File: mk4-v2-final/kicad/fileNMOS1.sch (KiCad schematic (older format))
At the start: 4 parts, among them Q1 Q_NMOS_GDS

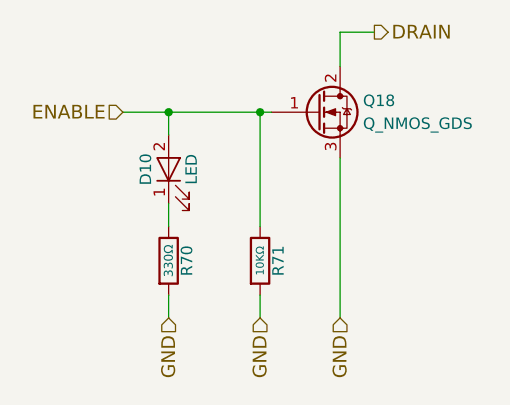
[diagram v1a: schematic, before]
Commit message: added headnight diodes, I don't think software control of them is going to be possible
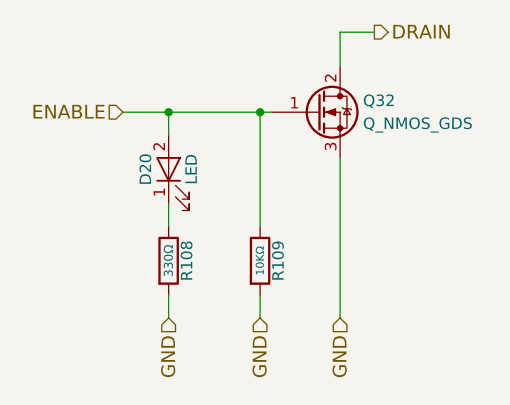
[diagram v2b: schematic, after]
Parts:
- renumbered D1 to D6, Q1 to Q7, R25 to R36, R26 to R37
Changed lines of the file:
@@
 ENABLE
 $Comp
-L R R26
+L R R37
 U 1 1 59DF0BE3
 P 5150 4900
-AR Path="/59DEA30F/5A0A2090/59DF0BE3" Ref="R26"  Part="1"
-AR Path="/59DEA30F/5A0A20A2/59DF0BE3" Ref="R28"  Part="1"
-AR Path="/59DEA30F/5A0A207D/59DF0BE3" Ref="R39"  Part="1"
-AR Path="/59DEA30F/5A282667/59DF0BE3" Ref="R69"  Part="1"
-AR Path="/59DEA30F/5A286B4A/59DF0BE3" Ref="R71"  Part="1"
-AR Path="/59DEA30F/5A1AB869/59DF0BE3" Ref="R73"  Part="1"
-AR Path="/59DEA30F/5A1AE2F5/59DF0BE3" Ref="R75"  Part="1"
-AR Path="/59DEA30F/5B17D435/59DF0BE3" Ref="R71"  Part="1"
-AR Path="/59DEA30F/5B17FE95/59DF0BE3" Ref="R71"  Part="1"
-F 0 "R71" V 5230 4900 50  0000 C CNN
+AR Path="/59DEA30F/5A0A207D/59DF0BE3" Ref="R37"  Part="1"
+AR Path="/59DEA30F/5A1AB869/59DF0BE3" Ref="R62"  Part="1"
+AR Path="/59DEA30F/5A1AE2F5/59DF0BE3" Ref="R64"  Part="1"
+AR Path="/59DEA30F/5B17D435/59DF0BE3" Ref="R107"  Part="1"
+AR Path="/59DEA30F/5B17FE95/59DF0BE3" Ref="R109"  Part="1"
+F 0 "R109" V 5230 4900 50  0000 C CNN
 F 1 "10KΩ" V 5150 4900 35  0000 C CNN
 F 2 "Resistors_THT:R_Axial_DIN0207_L6.3mm_D2.5mm_P10.16mm_Horizontal" V 5080 4900 50  0001 C CNN
@@
 GND
 $Comp
-L LED D1
+L LED D6
 U 1 1 5A613552
 P 4750 4500
-AR Path="/59DEA30F/5A0A2090/5A613552" Ref="D1"  Part="1"
-AR Path="/59DEA30F/5A0A20A2/5A613552" Ref="D2"  Part="1"
-AR Path="/59DEA30F/5A0A207D/5A613552" Ref="D5"  Part="1"
-AR Path="/59DEA30F/5A282667/5A613552" Ref="D9"  Part="1"
-AR Path="/59DEA30F/5A286B4A/5A613552" Ref="D10"  Part="1"
-AR Path="/59DEA30F/5A1AB869/5A613552" Ref="D11"  Part="1"
-AR Path="/59DEA30F/5A1AE2F5/5A613552" Ref="D12"  Part="1"
-AR Path="/59DEA30F/5B17D435/5A613552" Ref="D10"  Part="1"
-AR Path="/59DEA30F/5B17FE95/5A613552" Ref="D10"  Part="1"
-F 0 "D10" H 4750 4600 50  0000 C CNN
+AR Path="/59DEA30F/5A0A207D/5A613552" Ref="D6"  Part="1"
+AR Path="/59DEA30F/5A1AB869/5A613552" Ref="D9"  Part="1"
+AR Path="/59DEA30F/5A1AE2F5/5A613552" Ref="D10"  Part="1"
+AR Path="/59DEA30F/5B17D435/5A613552" Ref="D19"  Part="1"
+AR Path="/59DEA30F/5B17FE95/5A613552" Ref="D20"  Part="1"
+F 0 "D20" H 4750 4600 50  0000 C CNN
 F 1 "LED" H 4750 4400 50  0000 C CNN
 F 2 "LEDs:LED_D5.0mm" H 4750 4500 50  0001 C CNN
@@
 Connection ~ 4750 4250
 $Comp
-L R R25
+L R R36
 U 1 1 5A61355D
 P 4750 4900
-AR Path="/59DEA30F/5A0A2090/5A61355D" Ref="R25"  Part="1"
-AR Path="/59DEA30F/5A0A20A2/5A61355D" Ref="R27"  Part="1"
-AR Path="/59DEA30F/5A0A207D/5A61355D" Ref="R38"  Part="1"
-AR Path="/59DEA30F/5A282667/5A61355D" Ref="R68"  Part="1"
-AR Path="/59DEA30F/5A286B4A/5A61355D" Ref="R70"  Part="1"
-AR Path="/59DEA30F/5A1AB869/5A61355D" Ref="R72"  Part="1"
-AR Path="/59DEA30F/5A1AE2F5/5A61355D" Ref="R74"  Part="1"
-AR Path="/59DEA30F/5B17D435/5A61355D" Ref="R70"  Part="1"
-AR Path="/59DEA30F/5B17FE95/5A61355D" Ref="R70"  Part="1"
-F 0 "R70" V 4830 4900 50  0000 C CNN
+AR Path="/59DEA30F/5A0A207D/5A61355D" Ref="R36"  Part="1"
+AR Path="/59DEA30F/5A1AB869/5A61355D" Ref="R61"  Part="1"
+AR Path="/59DEA30F/5A1AE2F5/5A61355D" Ref="R63"  Part="1"
+AR Path="/59DEA30F/5B17D435/5A61355D" Ref="R106"  Part="1"
+AR Path="/59DEA30F/5B17FE95/5A61355D" Ref="R108"  Part="1"
+F 0 "R108" V 4830 4900 50  0000 C CNN
 F 1 "330Ω" V 4750 4900 39  0000 C CNN
 F 2 "Resistors_THT:R_Axial_DIN0207_L6.3mm_D2.5mm_P10.16mm_Horizontal" V 4680 4900 50  0001 C CNN
@@
 	5500 4450 5500 5150
 $Comp
-L Q_NMOS_GDS Q1
+L Q_NMOS_GDS Q7
 U 1 1 5A2ED2FC
 P 5400 4250
-AR Path="/59DEA30F/5A0A2090/5A2ED2FC" Ref="Q1"  Part="1"
-AR Path="/59DEA30F/5A0A20A2/5A2ED2FC" Ref="Q5"  Part="1"
-AR Path="/59DEA30F/5A0A207D/5A2ED2FC" Ref="Q9"  Part="1"
-AR Path="/59DEA30F/5A282667/5A2ED2FC" Ref="Q16"  Part="1"
-AR Path="/59DEA30F/5A286B4A/5A2ED2FC" Ref="Q18"  Part="1"
-AR Path="/59DEA30F/5A1AB869/5A2ED2FC" Ref="Q19"  Part="1"
-AR Path="/59DEA30F/5A1AE2F5/5A2ED2FC" Ref="Q20"  Part="1"
-AR Path="/59DEA30F/5B17D435/5A2ED2FC" Ref="Q18"  Part="1"
-AR Path="/59DEA30F/5B17FE95/5A2ED2FC" Ref="Q18"  Part="1"
-F 0 "Q18" H 5600 4300 50  0000 L CNN
+AR Path="/59DEA30F/5A0A207D/5A2ED2FC" Ref="Q7"  Part="1"
+AR Path="/59DEA30F/5A1AB869/5A2ED2FC" Ref="Q12"  Part="1"
+AR Path="/59DEA30F/5A1AE2F5/5A2ED2FC" Ref="Q13"  Part="1"
+AR Path="/59DEA30F/5B17D435/5A2ED2FC" Ref="Q31"  Part="1"
+AR Path="/59DEA30F/5B17FE95/5A2ED2FC" Ref="Q32"  Part="1"
+F 0 "Q32" H 5600 4300 50  0000 L CNN
 F 1 "Q_NMOS_GDS" H 5600 4200 50  0000 L CNN
 F 2 "TO_SOT_Packages_THT:TO-220-3_Vertical" H 5600 4350 50  0001 C CNN

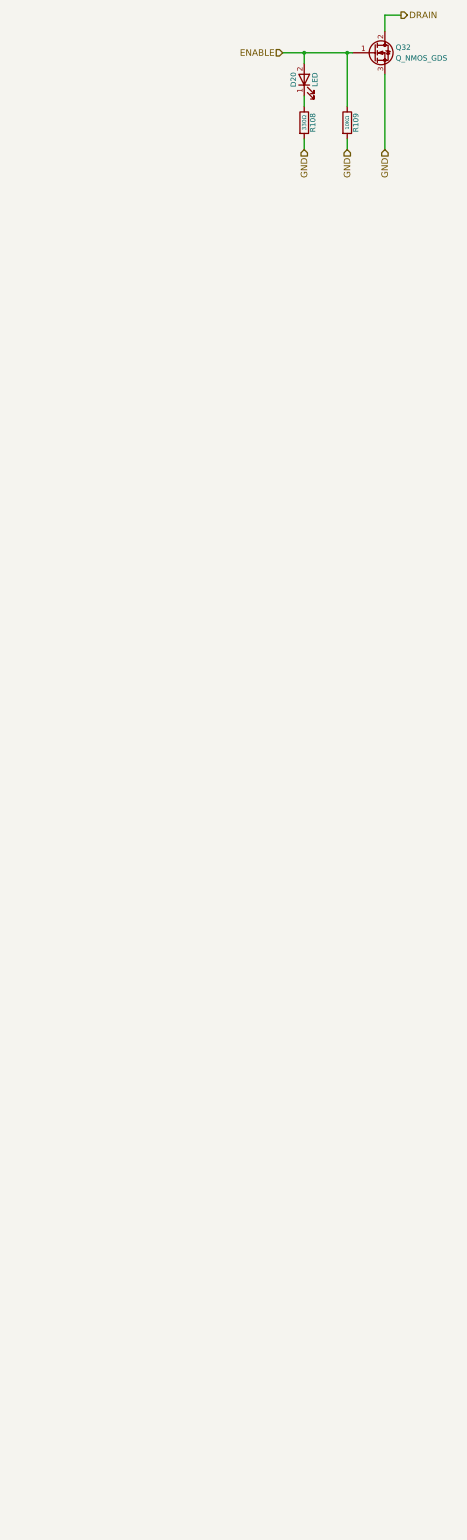
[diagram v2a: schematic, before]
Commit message: schematic is done, footprint association and netlist are also done
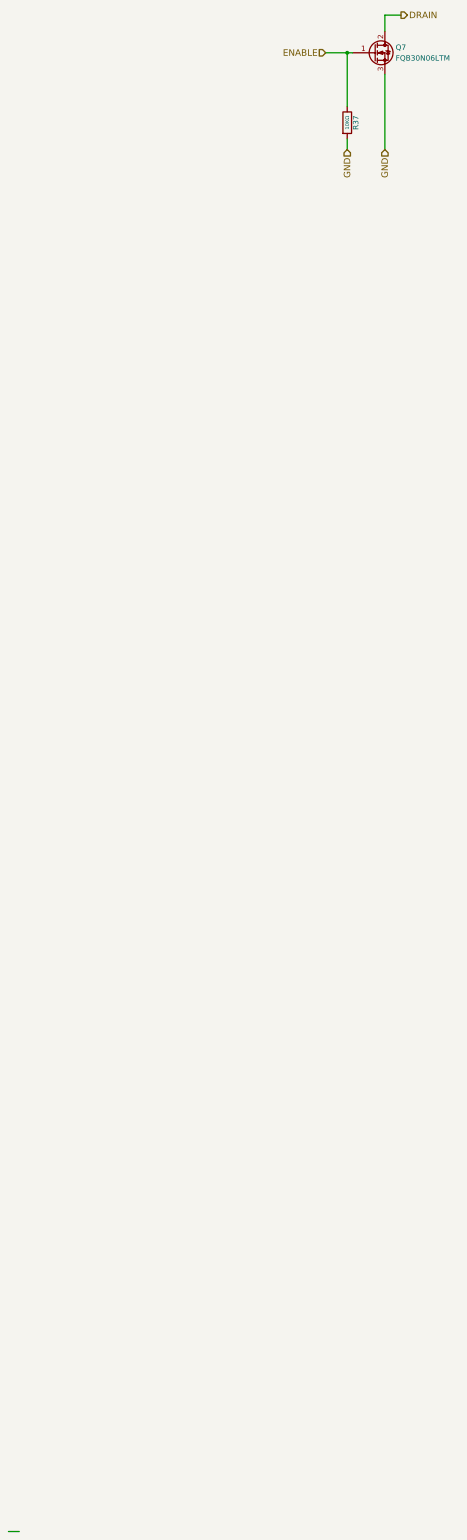
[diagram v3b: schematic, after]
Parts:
- removed D6: LED, LEDs:LED_D5.0mm, symbol LED
- removed R36: 330Ω, Resistors_THT:R_Axial_DIN0207_L6.3mm_D2.5mm_P10.16mm_Horizontal, symbol R
- Q7: value Q_NMOS_GDS -> FQB30N06LTM; footprint TO_SOT_Packages_THT:TO-220-3_Vertical -> TO_SOT_Packages_SMD:TO-263-3_TabPin2; digikey-pn (none) -> FQB30N06LTMCT-ND; mfg-pn (none) -> FQB30N06LTM
- R37: footprint Resistors_THT:R_Axial_DIN0207_L6.3mm_D2.5mm_P10.16mm_Horizontal -> Resistors_THT:R_Axial_DIN0204_L3.6mm_D1.6mm_P5.08mm_Horizontal; digikey-pn (none) -> BC10.0KXCT-ND; mfg-pn (none) -> MBA02040C1002FRP00
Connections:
- wire segments 9 -> 7
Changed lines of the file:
@@
 EESchema Schematic File Version 2
-LIBS:hitchco-mk4-rescue
 LIBS:power
 LIBS:device
@@
 LIBS:cd4013b
 LIBS:ncs3s1205sc
+LIBS:lca715
+LIBS:SN74HC595N
+LIBS:CD74HC4067
 LIBS:hitchco-mk4-cache
 EELAYER 25 0
@@
 $Descr USLetter 11000 8500
 encoding utf-8
-Sheet 12 54
+Sheet 15 54
 Title "sensor-mcu"
 Date "2017-10-11"
@@
 Comment4 ""
 $EndDescr
-Text HLabel 4550 4250 0    60   Input ~ 0
-ENABLE
 $Comp
 L R R37
@@
 AR Path="/59DEA30F/5B17D435/59DF0BE3" Ref="R107"  Part="1"
 AR Path="/59DEA30F/5B17FE95/59DF0BE3" Ref="R109"  Part="1"
-F 0 "R109" V 5230 4900 50  0000 C CNN
+F 0 "R37" V 5230 4900 50  0000 C CNN
 F 1 "10KΩ" V 5150 4900 35  0000 C CNN
-F 2 "Resistors_THT:R_Axial_DIN0207_L6.3mm_D2.5mm_P10.16mm_Horizontal" V 5080 4900 50  0001 C CNN
+F 2 "Resistors_THT:R_Axial_DIN0204_L3.6mm_D1.6mm_P5.08mm_Horizontal" V 5080 4900 50  0001 C CNN
 F 3 "" H 5150 4900 50  0001 C CNN
+F 4 "BC10.0KXCT-ND" H 5230 5000 50  0001 C CNN "digikey-pn"
+F 5 "MBA02040C1002FRP00" H 5230 5000 50  0001 C CNN "mfg-pn"
 	1    5150 4900
 	1    0    0    -1
 $EndComp
-Text HLabel 5650 3900 2    60   Output ~ 0
-DRAIN
-Wire Wire Line
-	4550 4250 5200 4250
-Wire Wire Line
-	5150 4250 5150 4750
-Connection ~ 5150 4250
-Wire Wire Line
-	5650 3900 5500 3900
-Wire Wire Line
-	5500 3900 5500 4050
-Text HLabel 5500 5150 3    60   Input ~ 0
-GND
-Text HLabel 5150 5150 3    60   Input ~ 0
-GND
-$Comp
-L LED D6
-U 1 1 5A613552
-P 4750 4500
-AR Path="/59DEA30F/5A0A207D/5A613552" Ref="D6"  Part="1"
-AR Path="/59DEA30F/5A1AB869/5A613552" Ref="D9"  Part="1"
-AR Path="/59DEA30F/5A1AE2F5/5A613552" Ref="D10"  Part="1"
-AR Path="/59DEA30F/5B17D435/5A613552" Ref="D19"  Part="1"
-AR Path="/59DEA30F/5B17FE95/5A613552" Ref="D20"  Part="1"
-F 0 "D20" H 4750 4600 50  0000 C CNN
-F 1 "LED" H 4750 4400 50  0000 C CNN
-F 2 "LEDs:LED_D5.0mm" H 4750 4500 50  0001 C CNN
-F 3 "http://www.kingbrightusa.com/images/catalog/SPEC/WP7113ID.pdf" H 4750 4500 50  0001 C CNN
-	1    4750 4500
-	0    -1   -1   0
-$EndComp
-Text HLabel 4750 5150 3    60   Input ~ 0
-GND
-Wire Wire Line
-	4750 4650 4750 4750
-Wire Wire Line
-	4750 4350 4750 4250
-Connection ~ 4750 4250
-$Comp
-L R R36
-U 1 1 5A61355D
-P 4750 4900
-AR Path="/59DEA30F/5A0A207D/5A61355D" Ref="R36"  Part="1"
-AR Path="/59DEA30F/5A1AB869/5A61355D" Ref="R61"  Part="1"
-AR Path="/59DEA30F/5A1AE2F5/5A61355D" Ref="R63"  Part="1"
-AR Path="/59DEA30F/5B17D435/5A61355D" Ref="R106"  Part="1"
-AR Path="/59DEA30F/5B17FE95/5A61355D" Ref="R108"  Part="1"
-F 0 "R108" V 4830 4900 50  0000 C CNN
-F 1 "330Ω" V 4750 4900 39  0000 C CNN
-F 2 "Resistors_THT:R_Axial_DIN0207_L6.3mm_D2.5mm_P10.16mm_Horizontal" V 4680 4900 50  0001 C CNN
-F 3 "" H 4750 4900 50  0001 C CNN
-	1    4750 4900
-	1    0    0    -1
-$EndComp
-Wire Wire Line
-	4750 5050 4750 5150
-Wire Wire Line
-	5150 5150 5150 5050
-Wire Wire Line
-	5500 4450 5500 5150
 $Comp
 L Q_NMOS_GDS Q7
@@
 AR Path="/59DEA30F/5B17D435/5A2ED2FC" Ref="Q31"  Part="1"
 AR Path="/59DEA30F/5B17FE95/5A2ED2FC" Ref="Q32"  Part="1"
-F 0 "Q32" H 5600 4300 50  0000 L CNN
-F 1 "Q_NMOS_GDS" H 5600 4200 50  0000 L CNN
-F 2 "TO_SOT_Packages_THT:TO-220-3_Vertical" H 5600 4350 50  0001 C CNN
-F 3 "" H 5400 4250 50  0001 C CNN
+F 0 "Q7" H 5600 4300 50  0000 L CNN
+F 1 "FQB30N06LTM" H 5600 4200 50  0000 L CNN
+F 2 "TO_SOT_Packages_SMD:TO-263-3_TabPin2" H 5600 4350 50  0001 C CNN
+F 3 "https://www.fairchildsemi.com/datasheets/FQ/FQB30N06L.pdf" H 5400 4250 50  0001 C CNN
+F 4 "FQB30N06LTMCT-ND" H 5600 4400 50  0001 C CNN "digikey-pn"
+F 5 "FQB30N06LTM" H 5600 4400 50  0001 C CNN "mfg-pn"
 	1    5400 4250
 	1    0    0    -1
 $EndComp
+Text HLabel 4950 4250 0    60   Input ~ 0
+ENABLE
+Text HLabel 5650 3900 2    60   Output ~ 0
+DRAIN
+Text HLabel 5500 5150 3    60   Input ~ 0
+GND
+Text HLabel 5150 5150 3    60   Input ~ 0
+GND
+Wire Wire Line
+	5150 4250 5150 4750
+Wire Wire Line
+	5650 3900 5500 3900
+Wire Wire Line
+	5500 3900 5500 4050
+Wire Wire Line
+	5150 5150 5150 5050
+Wire Wire Line
+	5500 4450 5500 5150
+Wire Wire Line
+	2000 18000 2100 18000
+Wire Wire Line
+	4950 4250 5200 4250
+Connection ~ 5150 4250
 $EndSCHEMATC

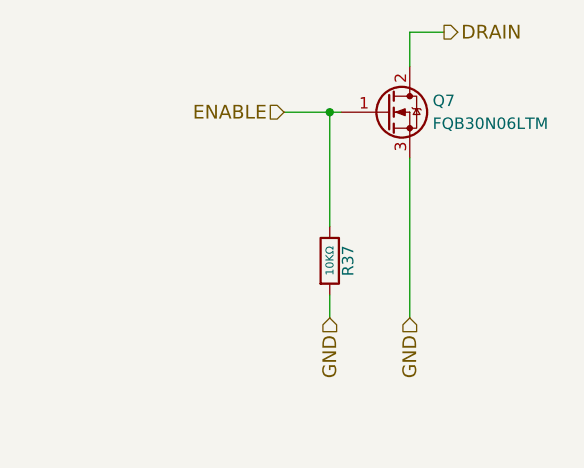
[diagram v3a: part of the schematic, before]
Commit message: all components on the board
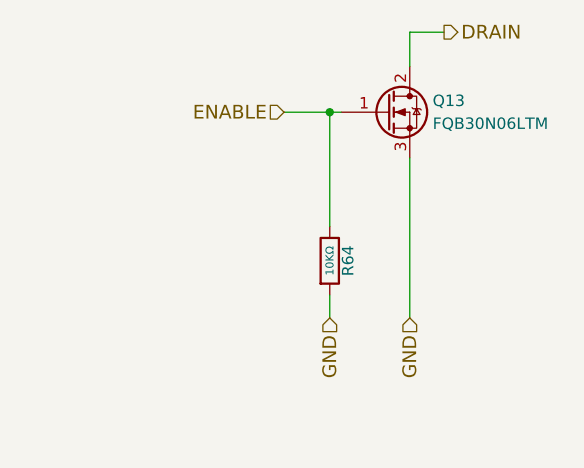
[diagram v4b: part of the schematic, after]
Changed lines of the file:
@@
 AR Path="/59DEA30F/5B17D435/59DF0BE3" Ref="R107"  Part="1"
 AR Path="/59DEA30F/5B17FE95/59DF0BE3" Ref="R109"  Part="1"
-F 0 "R37" V 5230 4900 50  0000 C CNN
+F 0 "R64" V 5230 4900 50  0000 C CNN
 F 1 "10KΩ" V 5150 4900 35  0000 C CNN
 F 2 "Resistors_THT:R_Axial_DIN0204_L3.6mm_D1.6mm_P5.08mm_Horizontal" V 5080 4900 50  0001 C CNN
@@
 AR Path="/59DEA30F/5B17D435/5A2ED2FC" Ref="Q31"  Part="1"
 AR Path="/59DEA30F/5B17FE95/5A2ED2FC" Ref="Q32"  Part="1"
-F 0 "Q7" H 5600 4300 50  0000 L CNN
+F 0 "Q13" H 5600 4300 50  0000 L CNN
 F 1 "FQB30N06LTM" H 5600 4200 50  0000 L CNN
 F 2 "TO_SOT_Packages_SMD:TO-263-3_TabPin2" H 5600 4350 50  0001 C CNN

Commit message: all files are in, time to order!
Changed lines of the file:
@@
 AR Path="/59DEA30F/5B17D435/59DF0BE3" Ref="R107"  Part="1"
 AR Path="/59DEA30F/5B17FE95/59DF0BE3" Ref="R109"  Part="1"
-F 0 "R64" V 5230 4900 50  0000 C CNN
+F 0 "R37" V 5230 4900 50  0000 C CNN
 F 1 "10KΩ" V 5150 4900 35  0000 C CNN
 F 2 "Resistors_THT:R_Axial_DIN0204_L3.6mm_D1.6mm_P5.08mm_Horizontal" V 5080 4900 50  0001 C CNN
@@
 AR Path="/59DEA30F/5B17D435/5A2ED2FC" Ref="Q31"  Part="1"
 AR Path="/59DEA30F/5B17FE95/5A2ED2FC" Ref="Q32"  Part="1"
-F 0 "Q13" H 5600 4300 50  0000 L CNN
+F 0 "Q7" H 5600 4300 50  0000 L CNN
 F 1 "FQB30N06LTM" H 5600 4200 50  0000 L CNN
 F 2 "TO_SOT_Packages_SMD:TO-263-3_TabPin2" H 5600 4350 50  0001 C CNN
